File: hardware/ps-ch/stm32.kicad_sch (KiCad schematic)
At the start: 15 parts, among them J1 Conn_02x05_Odd_Even, U12 STM32C031K4Tx

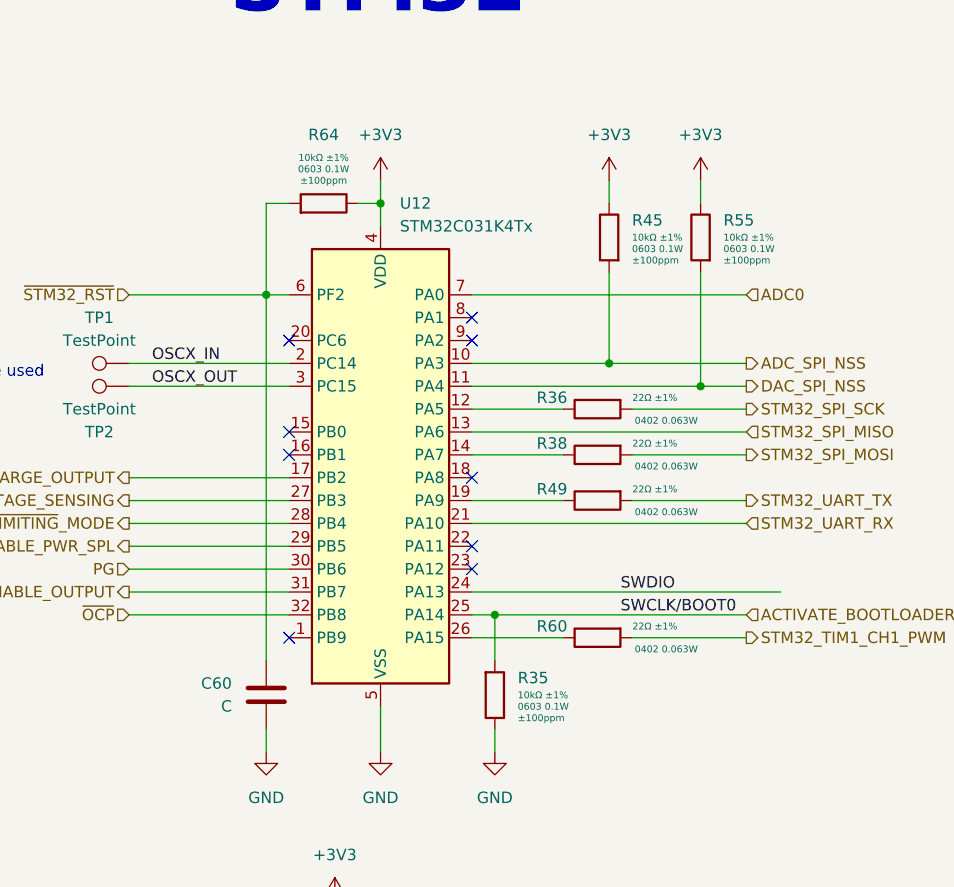
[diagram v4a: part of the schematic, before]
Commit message: calculated voltage correction
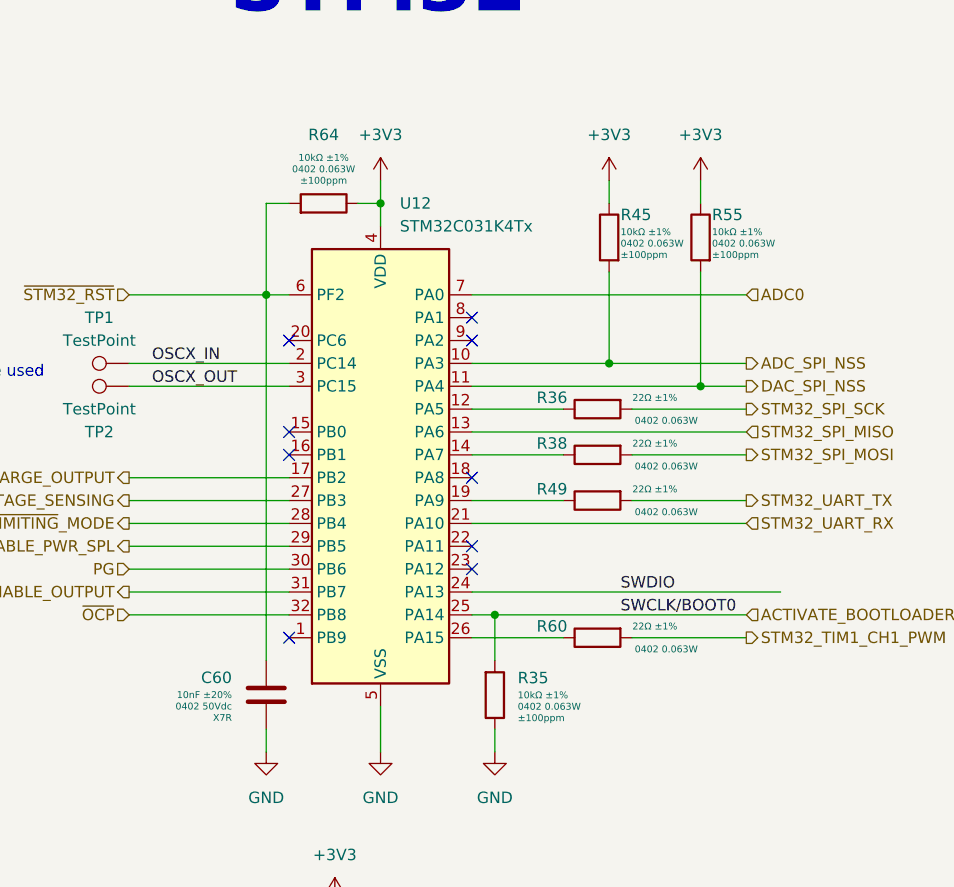
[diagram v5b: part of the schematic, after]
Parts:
- C60: value C -> 10nF 0402 50Vdc X7R ±20%; footprint (none) -> Capacitor_SMD:C_0402_1005Metric; symbol Device:C -> ps-ch:10nF 0402 50Vdc X7R ±20%; DisplayValue0 (none) -> 10nF ±20%; DisplayValue1 (none) -> 0402 50Vdc; DisplayValue2 (none) -> X7R; Manufacturer (none) -> Murata; Manufacturer Part Number (none) -> GRM155R71H103MA88
- R35, R45, R55, R64: value 10kΩ 0603 0.1W ±1% ±100ppm/°C -> 10kΩ 0402 0.063W ±1% ±100ppm/°C; footprint Resistor_SMD:R_0603_1608Metric -> Resistor_SMD:R_0402_1005Metric; symbol ps-ch:10kΩ 0603 0.1W ±1% ±100ppm/°C -> ps-ch:10kΩ 0402 0.063W ±1% ±100ppm/°C; DisplayValue1 0603 0.1W -> 0402 0.063W; Manufacturer Part Number AC0603FR-071K2L -> AC0402FR-0710KL
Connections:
- net GND: now also C60.1; no longer C60.2
- net ~{STM32_RST}: now also C60.2; no longer C60.1
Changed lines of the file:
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@@
 	)
 	(symbol
-		(lib_id "ps-ch:10kΩ 0603 0.1W ±1% ±100ppm/°C")
+		(lib_id "ps-ch:10kΩ 0402 0.063W ±1% ±100ppm/°C")
 		(at 156.21 110.49 0)
 		(unit 1)
@@
 			)
 		)
-		(property "Value" "10kΩ 0603 0.1W ±1% ±100ppm/°C"
+		(property "Value" "10kΩ 0402 0.063W ±1% ±100ppm/°C"
 			(at 156.21 96.266 0)
 			(effects
 				(font
-					(size 1 1)
-				)
-				(hide yes)
-			)
-		)
-		(property "Footprint" "Resistor_SMD:R_0603_1608Metric"
+					(size 1.27 1.27)
+				)
+				(hide yes)
+			)
+		)
+		(property "Footprint" "Resistor_SMD:R_0402_1005Metric"
 			(at 156.21 97.536 0)
 			(effects
 				(font
-					(size 1 1)
+					(size 1.27 1.27)
 				)
 				(hide yes)
@@
 			)
 		)
-		(property "Description" "R 0603 0.1W ±1% ±100ppm/°C"
+		(property "Description" "R 0402 0.063W ±1% ±100ppm/°C"
 			(at 156.21 99.06 0)
 			(effects
@@
 			(effects
 				(font
-					(size 1 1)
-				)
-				(hide yes)
-			)
-		)
-		(property "Manufacturer Part Number" "AC0603FR-071K2L"
+					(size 1.27 1.27)
+				)
+				(hide yes)
+			)
+		)
+		(property "Manufacturer Part Number" "AC0402FR-0710KL"
 			(at 156.21 93.726 0)
 			(effects
 				(font
-					(size 1 1)
+					(size 1.27 1.27)
 				)
 				(hide yes)
@@
 			)
 		)
-		(property "DisplayValue1" "0603 0.1W"
+		(property "DisplayValue1" "0402 0.063W"
 			(at 158.75 111.7854 0)
 			(effects
@@
 	)
 	(symbol
-		(lib_id "ps-ch:10kΩ 0603 0.1W ±1% ±100ppm/°C")
+		(lib_id "ps-ch:10kΩ 0402 0.063W ±1% ±100ppm/°C")
 		(at 179.07 59.69 180)
 		(unit 1)
@@
 		(on_board yes)
 		(dnp no)
-		(fields_autoplaced yes)
 		(property "Reference" "R55"
-			(at 181.61 57.7595 0)
+			(at 180.34 57.15 0)
 			(effects
 				(font
@@
 			)
 		)
-		(property "Value" "10kΩ 0603 0.1W ±1% ±100ppm/°C"
+		(property "Value" "10kΩ 0402 0.063W ±1% ±100ppm/°C"
 			(at 179.07 73.914 0)
 			(effects
 				(font
-					(size 1 1)
-				)
-				(hide yes)
-			)
-		)
-		(property "Footprint" "Resistor_SMD:R_0603_1608Metric"
+					(size 1.27 1.27)
+				)
+				(hide yes)
+			)
+		)
+		(property "Footprint" "Resistor_SMD:R_0402_1005Metric"
 			(at 179.07 72.644 0)
 			(effects
 				(font
-					(size 1 1)
+					(size 1.27 1.27)
 				)
 				(hide yes)
@@
 			)
 		)
-		(property "Description" "R 0603 0.1W ±1% ±100ppm/°C"
+		(property "Description" "R 0402 0.063W ±1% ±100ppm/°C"
 			(at 179.07 71.12 0)
 			(effects
@@
 			(effects
 				(font
-					(size 1 1)
-				)
-				(hide yes)
-			)
-		)
-		(property "Manufacturer Part Number" "AC0603FR-071K2L"
+					(size 1.27 1.27)
+				)
+				(hide yes)
+			)
+		)
+		(property "Manufacturer Part Number" "AC0402FR-0710KL"
 			(at 179.07 76.454 0)
 			(effects
 				(font
-					(size 1 1)
+					(size 1.27 1.27)
 				)
 				(hide yes)
@@
 		)
 		(property "DisplayValue0" "10kΩ ±1%"
-			(at 181.61 59.6646 0)
+			(at 180.34 59.0551 0)
 			(effects
 				(font
@@
 			)
 		)
-		(property "DisplayValue1" "0603 0.1W"
-			(at 181.61 60.9346 0)
+		(property "DisplayValue1" "0402 0.063W"
+			(at 180.34 60.3251 0)
 			(effects
 				(font
@@
 		)
 		(property "DisplayValue2" "±100ppm"
-			(at 181.61 62.2046 0)
+			(at 180.34 61.5951 0)
 			(effects
 				(font
@@
 	)
 	(symbol
-		(lib_id "ps-ch:10kΩ 0603 0.1W ±1% ±100ppm/°C")
+		(lib_id "ps-ch:10kΩ 0402 0.063W ±1% ±100ppm/°C")
 		(at 168.91 59.69 180)
 		(unit 1)
@@
 		(on_board yes)
 		(dnp no)
-		(fields_autoplaced yes)
 		(property "Reference" "R45"
-			(at 171.45 57.7595 0)
+			(at 170.18 57.15 0)
 			(effects
 				(font
@@
 			)
 		)
-		(property "Value" "10kΩ 0603 0.1W ±1% ±100ppm/°C"
+		(property "Value" "10kΩ 0402 0.063W ±1% ±100ppm/°C"
 			(at 168.91 73.914 0)
 			(effects
 				(font
-					(size 1 1)
-				)
-				(hide yes)
-			)
-		)
-		(property "Footprint" "Resistor_SMD:R_0603_1608Metric"
+					(size 1.27 1.27)
+				)
+				(hide yes)
+			)
+		)
+		(property "Footprint" "Resistor_SMD:R_0402_1005Metric"
 			(at 168.91 72.644 0)
 			(effects
 				(font
-					(size 1 1)
+					(size 1.27 1.27)
 				)
 				(hide yes)
@@
 			)
 		)
-		(property "Description" "R 0603 0.1W ±1% ±100ppm/°C"
+		(property "Description" "R 0402 0.063W ±1% ±100ppm/°C"
 			(at 168.91 71.12 0)
 			(effects
@@
 			(effects
 				(font
-					(size 1 1)
-				)
-				(hide yes)
-			)
-		)
-		(property "Manufacturer Part Number" "AC0603FR-071K2L"
+					(size 1.27 1.27)
+				)
+				(hide yes)
+			)
+		)
+		(property "Manufacturer Part Number" "AC0402FR-0710KL"
 			(at 168.91 76.454 0)
 			(effects
 				(font
-					(size 1 1)
+					(size 1.27 1.27)
 				)
 				(hide yes)
@@
 		)
 		(property "DisplayValue0" "10kΩ ±1%"
-			(at 171.45 59.6646 0)
+			(at 170.18 59.0551 0)
 			(effects
 				(font
@@
 			)
 		)
-		(property "DisplayValue1" "0603 0.1W"
-			(at 171.45 60.9346 0)
+		(property "DisplayValue1" "0402 0.063W"
+			(at 170.18 60.3251 0)
 			(effects
 				(font
@@
 		)
 		(property "DisplayValue2" "±100ppm"
-			(at 171.45 62.2046 0)
+			(at 170.18 61.5951 0)
 			(effects
 				(font
@@
 	)
 	(symbol
-		(lib_id "Device:C")
+		(lib_id "ps-ch:10nF 0402 50Vdc X7R ±20%")
 		(at 130.81 110.49 0)
 		(mirror y)
@@
 		(on_board yes)
 		(dnp no)
+		(fields_autoplaced yes)
 		(property "Reference" "C60"
-			(at 127 109.2199 0)
+			(at 127 108.5849 0)
 			(effects
 				(font
@@
 			)
 		)
-		(property "Value" "C"
+		(property "Value" "10nF 0402 50Vdc X7R ±20%"
 			(at 127 111.7599 0)
 			(effects
@@
 				)
 				(justify left)
-			)
-		)
-		(property "Footprint" ""
+				(hide yes)
+			)
+		)
+		(property "Footprint" "Capacitor_SMD:C_0402_1005Metric"
 			(at 129.8448 114.3 0)
 			(effects
@@
 			)
 		)
-		(property "Description" "Unpolarized capacitor"
+		(property "Description" "Capacitor 0402 50Vdc X7R ±20%"
 			(at 130.81 110.49 0)
 			(effects
@@
 				)
 				(hide yes)
+			)
+		)
+		(property "Manufacturer" "Murata"
+			(at 130.81 90.17 0)
+			(effects
+				(font
+					(size 1.27 1.27)
+				)
+				(hide yes)
+			)
+		)
+		(property "Manufacturer Part Number" "GRM155R71H103MA88"
+			(at 130.81 92.71 0)
+			(effects
+				(font
+					(size 1.27 1.27)
+				)
+				(hide yes)
+			)
+		)
+		(property "DisplayValue0" "10nF ±20%"
+			(at 127 110.49 0)
+			(effects
+				(font
+					(size 0.762 0.762)
+				)
+				(justify left)
+			)
+		)
+		(property "DisplayValue1" "0402 50Vdc"
+			(at 127 111.76 0)
+			(effects
+				(font
+					(size 0.762 0.762)
+				)
+				(justify left)
+			)
+		)
+		(property "DisplayValue2" "X7R"
+			(at 127 113.03 0)
+			(effects
+				(font
+					(size 0.762 0.762)
+				)
+				(justify left)
 			)
 		)
@@
 	)
 	(symbol
-		(lib_id "ps-ch:10kΩ 0603 0.1W ±1% ±100ppm/°C")
+		(lib_id "ps-ch:10kΩ 0402 0.063W ±1% ±100ppm/°C")
 		(at 137.16 55.88 90)
 		(unit 1)
@@
 			)
 		)
-		(property "Value" "10kΩ 0603 0.1W ±1% ±100ppm/°C"
+		(property "Value" "10kΩ 0402 0.063W ±1% ±100ppm/°C"
 			(at 122.936 55.88 0)
 			(effects
 				(font
-					(size 1 1)
-				)
-				(hide yes)
-			)
-		)
-		(property "Footprint" "Resistor_SMD:R_0603_1608Metric"
+					(size 1.27 1.27)
+				)
+				(hide yes)
+			)
+		)
+		(property "Footprint" "Resistor_SMD:R_0402_1005Metric"
 			(at 124.206 55.88 0)
 			(effects
 				(font
-					(size 1 1)
+					(size 1.27 1.27)
 				)
 				(hide yes)
@@
 			)
 		)
-		(property "Description" "R 0603 0.1W ±1% ±100ppm/°C"
+		(property "Description" "R 0402 0.063W ±1% ±100ppm/°C"
 			(at 125.73 55.88 0)
 			(effects
@@
 			(effects
 				(font
-					(size 1 1)
-				)
-				(hide yes)
-			)
-		)
-		(property "Manufacturer Part Number" "AC0603FR-071K2L"
+					(size 1.27 1.27)
+				)
+				(hide yes)
+			)
+		)
+		(property "Manufacturer Part Number" "AC0402FR-0710KL"
 			(at 120.396 55.88 0)
 			(effects
 				(font
-					(size 1 1)
+					(size 1.27 1.27)
 				)
 				(hide yes)
@@
 			)
 		)
-		(property "DisplayValue1" "0603 0.1W"
+		(property "DisplayValue1" "0402 0.063W"
 			(at 137.1854 52.07 90)
 			(effects

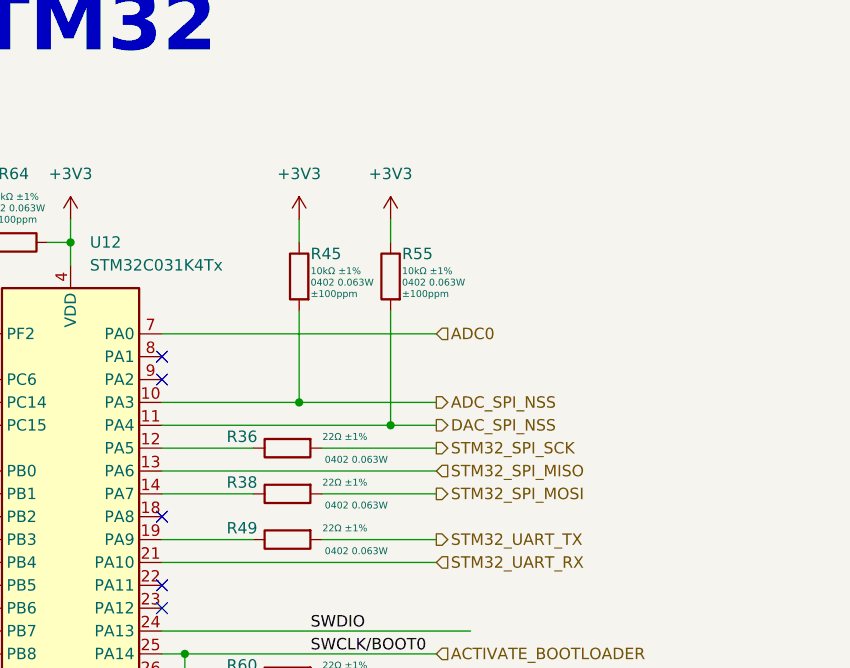
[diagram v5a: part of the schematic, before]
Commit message: assigned footprints
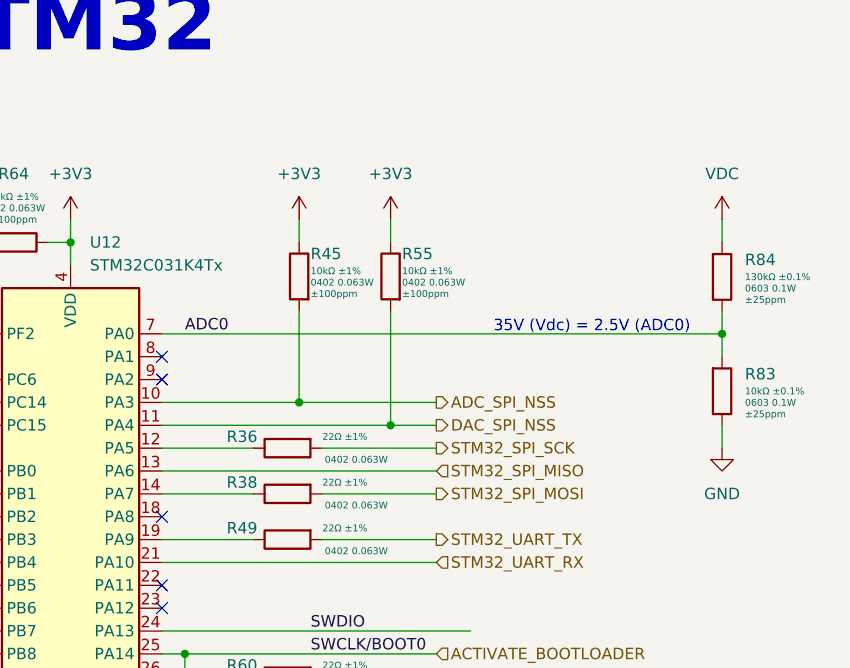
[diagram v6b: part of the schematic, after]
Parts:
- added R83: 10kΩ 0402 0.063W ±1% ±100ppm/°C, Resistor_SMD:R_0603_1608Metric, symbol ps-ch:10kΩ 0603 0.1W ±0.1% ±25ppm/°C
- added R84: 10kΩ 0402 0.063W ±1% ±100ppm/°C, Resistor_SMD:R_0603_1608Metric, symbol ps-ch:130kΩ 0603 0.1W ±0.1% ±25ppm/°C
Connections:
- net ADC0: now also R83.2, R84.1
- net GND: now also R83.1
- new net VDC: R84.2
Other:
- note added: "35V (Vdc) = 2.5V (ADC0)"

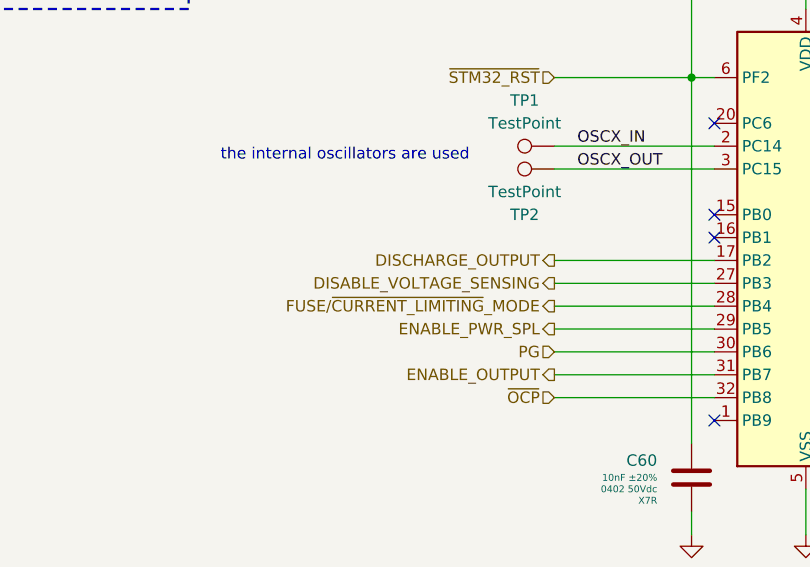
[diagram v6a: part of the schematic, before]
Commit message: changed voltage sensing circuit
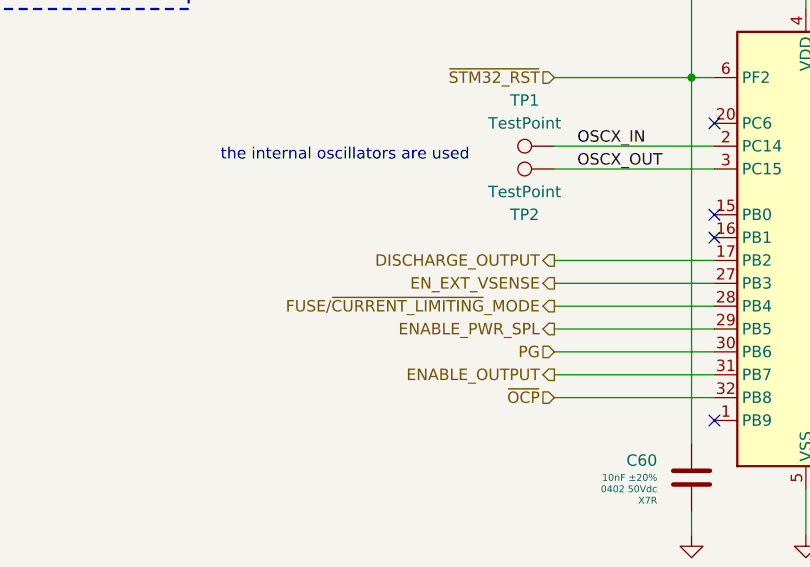
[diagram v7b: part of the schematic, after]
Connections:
- net DISABLE_VOLTAGE_SENSING renamed EN_EXT_VSENSE
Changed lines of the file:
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@@
 		)
 	)
-	(hierarchical_label "DISABLE_VOLTAGE_SENSING"
+	(hierarchical_label "EN_EXT_VSENSE"
 		(shape output)
 		(at 115.57 88.9 180)

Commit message: created and assigned footprints
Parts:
- TP1, TP2: footprint (none) -> TestPoint:TestPoint_Pad_D1.0mm
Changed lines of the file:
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@@
 			)
 		)
-		(property "Footprint" ""
+		(property "Footprint" "TestPoint:TestPoint_Pad_D1.0mm"
 			(at 115.57 68.58 0)
 			(effects
@@
 			)
 		)
-		(property "Footprint" ""
+		(property "Footprint" "TestPoint:TestPoint_Pad_D1.0mm"
 			(at 115.57 81.28 0)
 			(effects
